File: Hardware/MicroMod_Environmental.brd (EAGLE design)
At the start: 65 x 38 mm, 56 parts, among them J1 MICROMOD_STANDARD, U1 SGP40, U2 EEPROM, U3 SHTC3, U4 3.3V, U5 STC31

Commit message: Adds pullup and jumper to the EEPROM's write protect, brings WP pin to card's edge
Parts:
- added JP2: JUMPER-SMT_2_NO_SILK, SparkFun-Jumpers:SMT-JUMPER_2_NO_SILK
- added R8: 10k, SparkFun-Resistors:0603
- added U$23: (no value), top:#WP#403132222525
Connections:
- new net WP: J1.40, JP2.2, R8.1, U2.7
- net 3.3V: now also R8.2
- net GND: now also JP2.1; no longer U2.7
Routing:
- net WP: track 0.00 -> 23.4 mm, vias 0 -> 1
- net 3.3V: track 115.8 -> 116.6 mm
- net GND: vias 24 -> 23
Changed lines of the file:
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@@
 <element name="U$22" library="top" package="STC313502" value="" x="42.6212" y="16.129" smashed="yes"/>
 <element name="LOGO3" library="SparkFun-Aesthetics" package="ORDERING_INSTRUCTIONS" value="SPECIAL_INSTRUCTIONS-ORDERING" x="80.01" y="50.8" smashed="yes"/>
+<element name="R8" library="SparkFun-Resistors" package="0603" value="10k" x="15.875" y="20.447" smashed="yes" rot="R90">
+<attribute name="NAME" x="15.113" y="20.447" size="0.6096" layer="25" font="vector" ratio="20" rot="R90" align="bottom-center"/>
+<attribute name="PROD_ID" value="RES-00824" x="15.875" y="20.447" size="1.778" layer="27" font="vector" ratio="15" rot="R90" display="off"/>
+<attribute name="VALUE" x="16.637" y="20.447" size="0.6096" layer="27" font="vector" ratio="20" rot="R90" align="top-center"/>
+</element>
+<element name="JP2" library="SparkFun-Jumpers" package="SMT-JUMPER_2_NO_SILK" package3d_urn="urn:adsk.eagle:package:39279/1" value="JUMPER-SMT_2_NO_SILK" x="11.43" y="24.13" smashed="yes">
+<attribute name="NAME" x="11.43" y="25.273" size="0.6096" layer="25" font="vector" ratio="20" align="bottom-center"/>
+<attribute name="VALUE" x="11.43" y="22.987" size="0.6096" layer="27" font="vector" ratio="20" align="top-center"/>
+</element>
+<element name="U$23" library="top" package="#WP#403132222525" value="" x="9.144" y="24.13" smashed="yes"/>
 </elements>
 <signals>
@@
 <contactref element="J1" pad="GND1"/>
 <contactref element="U2" pad="4"/>
-<contactref element="U2" pad="7"/>
 <polygon width="0.254" layer="16" isolate="0.2032" rank="4">
 <vertex x="0" y="38.1"/>
@@
 <via x="6.9342" y="17.272" extent="1-16" drill="0.3048"/>
 <via x="3.4544" y="20.0914" extent="1-16" drill="0.3048"/>
-<via x="15.6972" y="19.6088" extent="1-16" drill="0.3048"/>
 <wire x1="1.275" y1="19.3" x2="2.54" y2="19.3" width="0.254" layer="1"/>
 <wire x1="2.54" y1="19.3" x2="2.663" y2="19.3" width="0.254" layer="1"/>
@@
 <via x="37.4142" y="17.018" extent="1-16" drill="0.3048"/>
 <via x="6.1214" y="20.9804" extent="1-16" drill="0.3048"/>
+<contactref element="JP2" pad="1"/>
 </signal>
 <signal name="3.3V" class="2">
@@
 <contactref element="JP1" pad="2"/>
 <contactref element="U2" pad="8"/>
-<wire x1="14.2541" y1="30.16" x2="15.5448" y2="30.16" width="0.3048" layer="1"/>
-<wire x1="15.5448" y1="30.16" x2="16.405" y2="30.16" width="0.3048" layer="1"/>
+<wire x1="14.2541" y1="30.16" x2="16.405" y2="30.16" width="0.3048" layer="1"/>
 <wire x1="16.405" y1="30.16" x2="16.637" y2="30.392" width="0.3048" layer="1"/>
 <via x="24.13" y="25.908" extent="1-16" drill="0.3048"/>
@@
 <vertex x="41.1734" y="18.1356"/>
 </polygon>
-<wire x1="15.5448" y1="30.16" x2="15.5448" y2="21.1328" width="0.3048" layer="1"/>
-<wire x1="15.367" y1="20.955" x2="14.23" y2="20.955" width="0.3048" layer="1"/>
-<wire x1="15.5448" y1="21.1328" x2="15.367" y2="20.955" width="0.3048" layer="1"/>
 <contactref element="PWR\" pad="2"/>
 <wire x1="24.9428" y1="34.0614" x2="56.2864" y2="34.0614" width="0.254" layer="1"/>
@@
 <wire x1="24.169" y1="30.519" x2="24.0225" y2="30.3725" width="0.3048" layer="1"/>
 <wire x1="24.169" y1="27.6352" x2="24.169" y2="30.226" width="0.3048" layer="1"/>
+<contactref element="R8" pad="2"/>
+<wire x1="14.23" y1="20.955" x2="15.533" y2="20.955" width="0.254" layer="1"/>
+<wire x1="15.533" y1="20.955" x2="15.875" y2="21.297" width="0.254" layer="1"/>
+<wire x1="15.875" y1="21.297" x2="16.637" y2="22.059" width="0.254" layer="1"/>
+<wire x1="16.637" y1="22.059" x2="16.637" y2="30.392" width="0.254" layer="1"/>
 </signal>
 <signal name="EN">
@@
 <contactref element="U2" pad="1"/>
 <contactref element="J1" pad="36"/>
-<wire x1="1.525" y1="18.55" x2="4.834" y2="18.55" width="0.2032" layer="16"/>
+<wire x1="1.525" y1="18.55" x2="3.81" y2="18.55" width="0.2032" layer="16"/>
+<wire x1="3.81" y1="18.55" x2="4.834" y2="18.55" width="0.2032" layer="16"/>
 <wire x1="4.834" y1="18.55" x2="7.112" y2="20.828" width="0.2032" layer="16"/>
 <via x="7.112" y="20.828" extent="1-16" drill="0.3048"/>
@@
 <wire x1="8.503" y1="19.558" x2="8.63" y2="19.685" width="0.2032" layer="1"/>
 </signal>
+<signal name="WP">
+<contactref element="J1" pad="40"/>
+<contactref element="U2" pad="7"/>
+<contactref element="R8" pad="1"/>
+<contactref element="JP2" pad="2"/>
+<wire x1="14.23" y1="19.685" x2="15.787" y2="19.685" width="0.254" layer="1"/>
+<wire x1="15.787" y1="19.685" x2="15.875" y2="19.597" width="0.254" layer="1"/>
+<wire x1="1.525" y1="19.55" x2="4.31" y2="19.55" width="0.2032" layer="16"/>
+<wire x1="4.31" y1="19.55" x2="5.08" y2="20.32" width="0.2032" layer="16"/>
+<wire x1="5.08" y1="20.32" x2="5.08" y2="21.59" width="0.2032" layer="16"/>
+<wire x1="5.08" y1="21.59" x2="7.62" y2="24.13" width="0.2032" layer="16"/>
+<via x="12.7" y="24.13" extent="1-16" drill="0.3048"/>
+<wire x1="12.7" y1="24.13" x2="11.8364" y2="24.13" width="0.2032" layer="1"/>
+<wire x1="7.62" y1="24.13" x2="12.7" y2="24.13" width="0.2032" layer="16"/>
+<wire x1="14.23" y1="19.685" x2="12.065" y2="19.685" width="0.2032" layer="1"/>
+<wire x1="12.065" y1="19.685" x2="11.43" y2="20.32" width="0.2032" layer="1"/>
+<wire x1="11.43" y1="20.32" x2="11.43" y2="22.86" width="0.2032" layer="1"/>
+<wire x1="11.684" y1="23.114" x2="11.43" y2="22.86" width="0.2032" layer="1"/>
+<wire x1="11.8364" y1="23.2664" x2="11.8364" y2="24.13" width="0.2032" layer="1"/>
+<wire x1="11.684" y1="23.114" x2="11.8364" y2="23.2664" width="0.2032" layer="1"/>
+</signal>
 </signals>

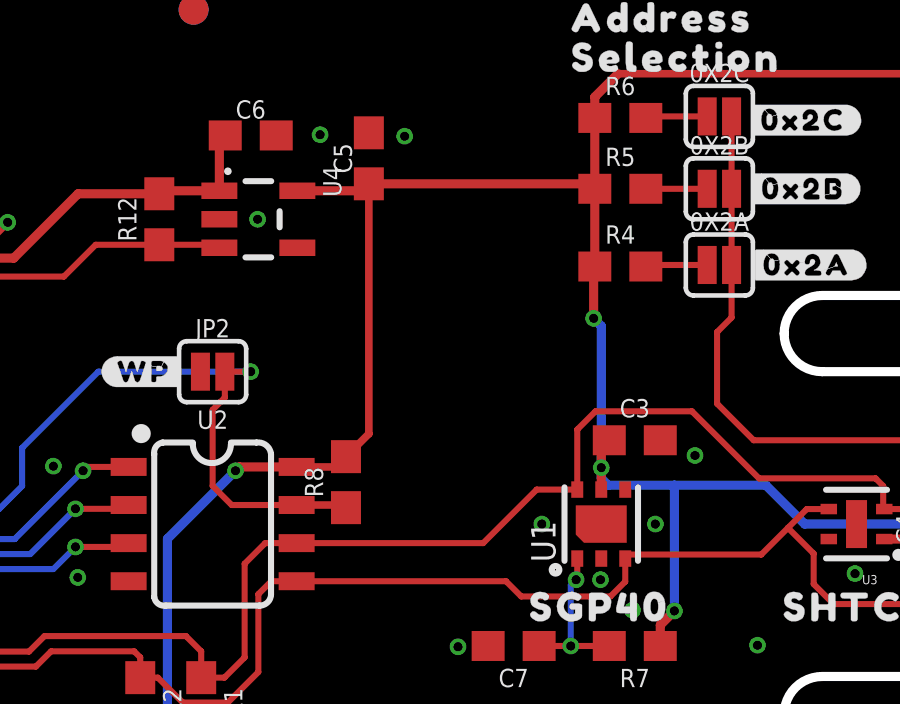
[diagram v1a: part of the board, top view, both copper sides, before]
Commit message: Updates pull up resistors to 2.2k from 4.7k
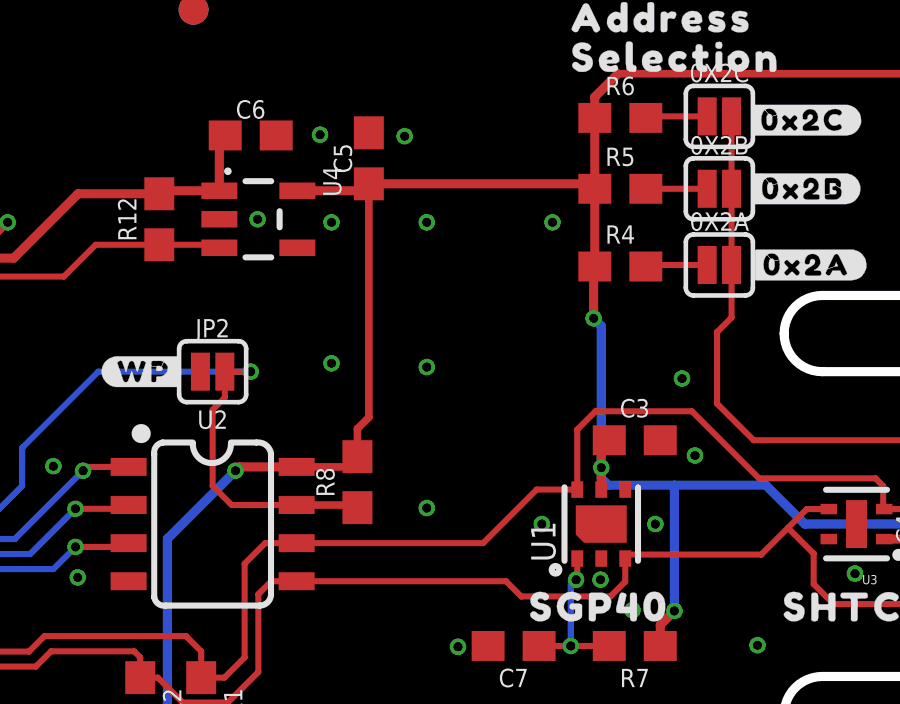
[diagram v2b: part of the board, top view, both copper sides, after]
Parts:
- R1, R2: value 4.7k -> 2.2k
- moved R8 0.38 mm to (16.3, 20.4)
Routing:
- net GND: vias 23 -> 30
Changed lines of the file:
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@@
 </element>
 <element name="J1" library="SparkFun-MicroMod-Function" package="M.2-CARD-E-22_FUNCTION_STANDARD" value="MICROMOD_STANDARD" x="0" y="19.05" smashed="yes" rot="R270"/>
-<element name="R1" library="SparkFun-Resistors" package="0603" value="4.7k" x="11.049" y="13.081" smashed="yes" rot="R270">
+<element name="R1" library="SparkFun-Resistors" package="0603" value="2.2k" x="11.049" y="13.081" smashed="yes" rot="R270">
 <attribute name="NAME" x="11.811" y="13.081" size="0.6096" layer="25" font="vector" ratio="20" rot="R270" align="bottom-center"/>
-<attribute name="PROD_ID" value="RES-07857" x="11.049" y="13.081" size="1.778" layer="27" font="vector" ratio="15" rot="R270" display="off"/>
-<attribute name="VALUE" x="10.287" y="13.081" size="0.6096" layer="27" font="vector" ratio="20" rot="R270" align="top-center"/>
-</element>
-<element name="R2" library="SparkFun-Resistors" package="0603" value="4.7k" x="9.017" y="13.081" smashed="yes" rot="R270">
+<attribute name="PROD_ID" value="RES-08272" x="11.049" y="13.081" size="1.778" layer="27" font="vector" ratio="15" rot="R270" display="off"/>
+<attribute name="VALUE" value="2.2k" x="10.287" y="13.081" size="0.6096" layer="27" font="vector" ratio="20" rot="R270" align="top-center"/>
+</element>
+<element name="R2" library="SparkFun-Resistors" package="0603" value="2.2k" x="9.017" y="13.081" smashed="yes" rot="R270">
 <attribute name="NAME" x="9.779" y="13.081" size="0.6096" layer="25" font="vector" ratio="20" rot="R270" align="bottom-center"/>
-<attribute name="PROD_ID" value="RES-07857" x="9.017" y="13.081" size="1.778" layer="27" font="vector" ratio="15" rot="R270" display="off"/>
-<attribute name="VALUE" x="8.255" y="13.081" size="0.6096" layer="27" font="vector" ratio="20" rot="R270" align="top-center"/>
+<attribute name="PROD_ID" value="RES-08272" x="9.017" y="13.081" size="1.778" layer="27" font="vector" ratio="15" rot="R270" display="off"/>
+<attribute name="VALUE" value="2.2k" x="8.255" y="13.081" size="0.6096" layer="27" font="vector" ratio="20" rot="R270" align="top-center"/>
 </element>
 <element name="C5" library="SparkFun-Capacitors" package="0603" value="1.0uF" x="16.637" y="31.242" smashed="yes" rot="R90">
@@
 <element name="U$22" library="top" package="STC313502" value="" x="42.6212" y="16.129" smashed="yes"/>
 <element name="LOGO3" library="SparkFun-Aesthetics" package="ORDERING_INSTRUCTIONS" value="SPECIAL_INSTRUCTIONS-ORDERING" x="80.01" y="50.8" smashed="yes"/>
-<element name="R8" library="SparkFun-Resistors" package="0603" value="10k" x="15.875" y="20.447" smashed="yes" rot="R90">
-<attribute name="NAME" x="15.113" y="20.447" size="0.6096" layer="25" font="vector" ratio="20" rot="R90" align="bottom-center"/>
-<attribute name="PROD_ID" value="RES-00824" x="15.875" y="20.447" size="1.778" layer="27" font="vector" ratio="15" rot="R90" display="off"/>
-<attribute name="VALUE" x="16.637" y="20.447" size="0.6096" layer="27" font="vector" ratio="20" rot="R90" align="top-center"/>
+<element name="R8" library="SparkFun-Resistors" package="0603" value="10k" x="16.256" y="20.447" smashed="yes" rot="R90">
+<attribute name="NAME" x="15.494" y="20.447" size="0.6096" layer="25" font="vector" ratio="20" rot="R90" align="bottom-center"/>
+<attribute name="PROD_ID" value="RES-00824" x="16.256" y="20.447" size="1.778" layer="27" font="vector" ratio="15" rot="R90" display="off"/>
+<attribute name="VALUE" x="17.018" y="20.447" size="0.6096" layer="27" font="vector" ratio="20" rot="R90" align="top-center"/>
 </element>
 <element name="JP2" library="SparkFun-Jumpers" package="SMT-JUMPER_2_NO_SILK" package3d_urn="urn:adsk.eagle:package:39279/1" value="JUMPER-SMT_2_NO_SILK" x="11.43" y="24.13" smashed="yes">
@@
 <via x="6.1214" y="20.9804" extent="1-16" drill="0.3048"/>
 <contactref element="JP2" pad="1"/>
+<via x="18.5674" y="19.5834" extent="1-16" drill="0.3048"/>
+<via x="18.5674" y="29.1084" extent="1-16" drill="0.3048"/>
+<via x="22.7584" y="29.1084" extent="1-16" drill="0.3048"/>
+<via x="27.0764" y="23.9014" extent="1-16" drill="0.3048"/>
+<via x="18.5674" y="24.2824" extent="1-16" drill="0.3048"/>
+<via x="15.3924" y="24.4094" extent="1-16" drill="0.3048"/>
+<via x="15.3924" y="29.1084" extent="1-16" drill="0.3048"/>
 </signal>
 <signal name="3.3V" class="2">
@@
 <wire x1="24.169" y1="27.6352" x2="24.169" y2="30.226" width="0.3048" layer="1"/>
 <contactref element="R8" pad="2"/>
-<wire x1="14.23" y1="20.955" x2="15.533" y2="20.955" width="0.254" layer="1"/>
-<wire x1="15.533" y1="20.955" x2="15.875" y2="21.297" width="0.254" layer="1"/>
-<wire x1="15.875" y1="21.297" x2="16.637" y2="22.059" width="0.254" layer="1"/>
-<wire x1="16.637" y1="22.059" x2="16.637" y2="30.392" width="0.254" layer="1"/>
+<wire x1="14.23" y1="20.955" x2="15.914" y2="20.955" width="0.254" layer="1"/>
+<wire x1="15.914" y1="20.955" x2="16.256" y2="21.297" width="0.254" layer="1"/>
+<wire x1="16.637" y1="22.606" x2="16.637" y2="30.392" width="0.254" layer="1"/>
+<wire x1="16.256" y1="21.297" x2="16.256" y2="22.225" width="0.254" layer="1"/>
+<wire x1="16.256" y1="22.225" x2="16.637" y2="22.606" width="0.254" layer="1"/>
 </signal>
 <signal name="EN">
@@
 <contactref element="R8" pad="1"/>
 <contactref element="JP2" pad="2"/>
-<wire x1="14.23" y1="19.685" x2="15.787" y2="19.685" width="0.254" layer="1"/>
-<wire x1="15.787" y1="19.685" x2="15.875" y2="19.597" width="0.254" layer="1"/>
+<wire x1="14.23" y1="19.685" x2="16.168" y2="19.685" width="0.254" layer="1"/>
+<wire x1="16.168" y1="19.685" x2="16.256" y2="19.597" width="0.254" layer="1"/>
 <wire x1="1.525" y1="19.55" x2="4.31" y2="19.55" width="0.2032" layer="16"/>
 <wire x1="4.31" y1="19.55" x2="5.08" y2="20.32" width="0.2032" layer="16"/>
@@
 <wire x1="12.065" y1="19.685" x2="11.43" y2="20.32" width="0.2032" layer="1"/>
 <wire x1="11.43" y1="20.32" x2="11.43" y2="22.86" width="0.2032" layer="1"/>
-<wire x1="11.684" y1="23.114" x2="11.43" y2="22.86" width="0.2032" layer="1"/>
+<wire x1="11.8364" y1="23.2664" x2="11.43" y2="22.86" width="0.2032" layer="1"/>
 <wire x1="11.8364" y1="23.2664" x2="11.8364" y2="24.13" width="0.2032" layer="1"/>
-<wire x1="11.684" y1="23.114" x2="11.8364" y2="23.2664" width="0.2032" layer="1"/>
 </signal>
 </signals>
